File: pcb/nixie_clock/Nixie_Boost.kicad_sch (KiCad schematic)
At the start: 0 parts

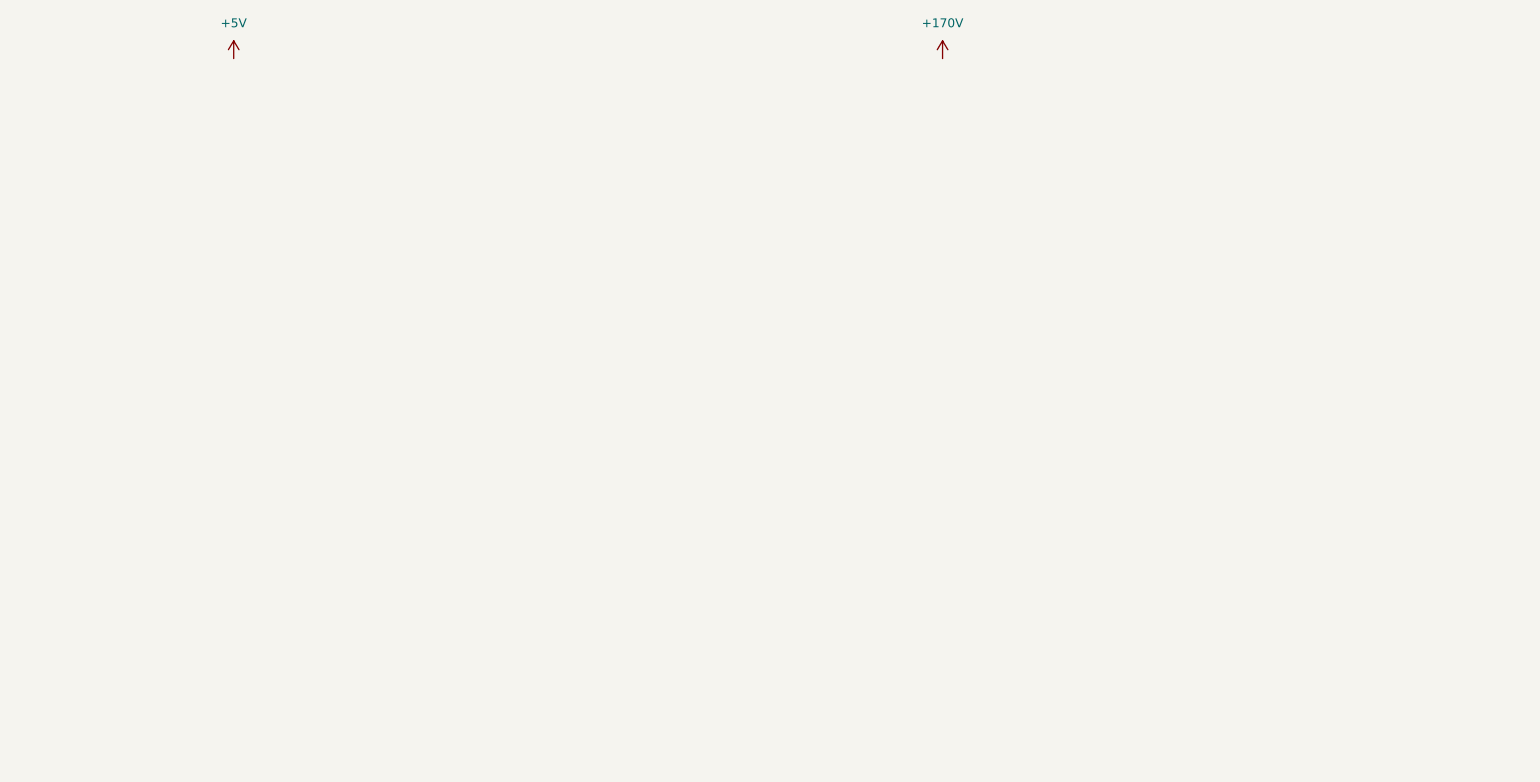
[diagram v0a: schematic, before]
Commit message: schematic finalisation, footprint assignment and start on placeing components in layout.
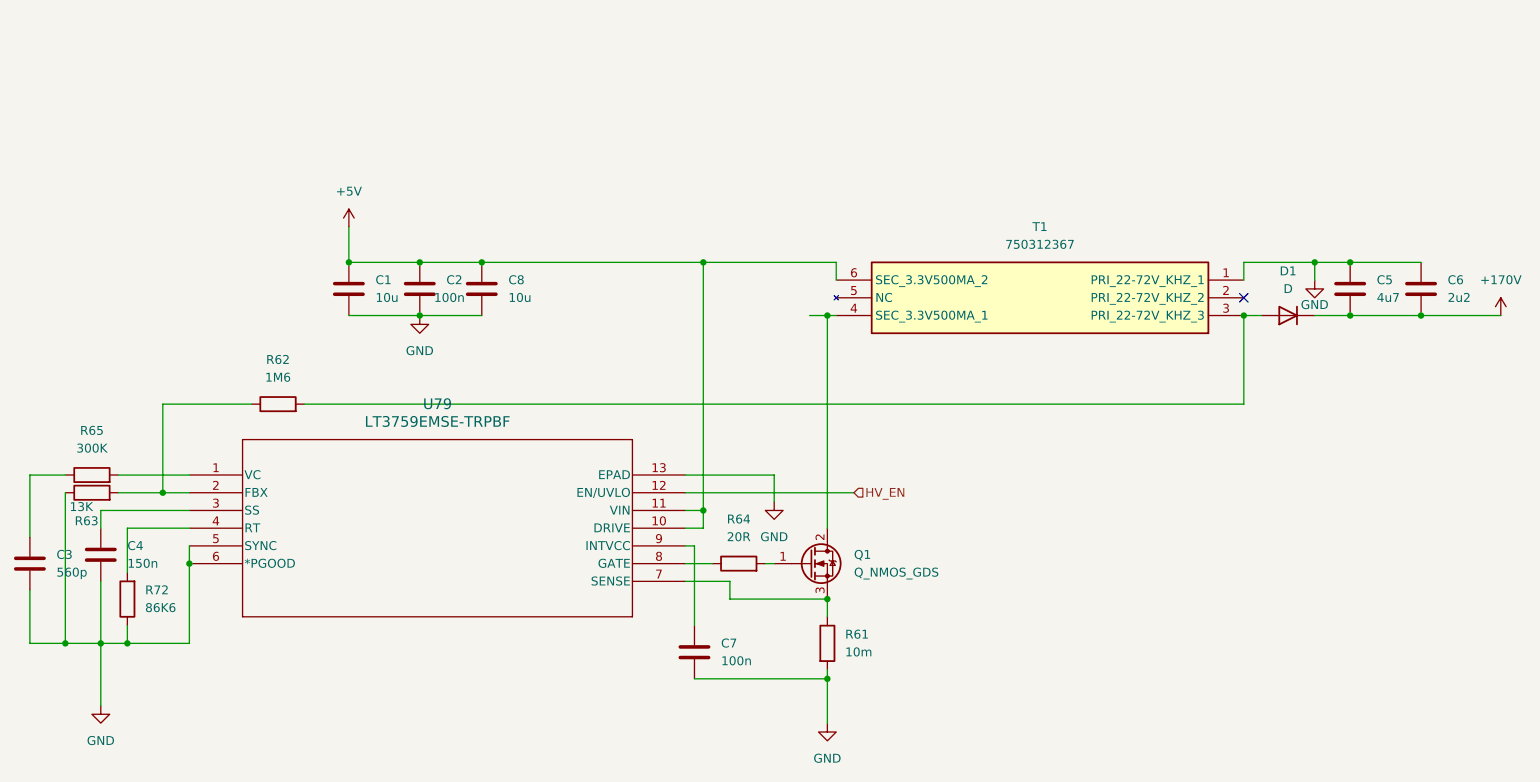
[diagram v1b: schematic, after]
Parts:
- added C1, C8: 10u, Capacitor_SMD:C_1210_3225Metric, symbol Device:C
- added C2: 100n, Capacitor_SMD:C_0805_2012Metric, symbol Device:C
- added C3: 560p, Capacitor_SMD:C_0603_1608Metric, symbol Device:C
- added C4: 150n, Capacitor_SMD:C_0603_1608Metric, symbol Device:C
- added C5: 4u7, Capacitor_SMD:C_0603_1608Metric, symbol Device:C
- added C6: 2u2, Capacitor_SMD:C_2220_5750Metric, symbol Device:C
- added C7: 100n, Capacitor_SMD:C_1812_4532Metric, symbol Device:C
- added D1: D, Capacitor_SMD:C_1812_4532Metric, symbol Device:D
- added Q1: Q_NMOS_GDS, Package_TO_SOT_SMD:LFPAK56, symbol Device:Q_NMOS_GDS
- added R61: 10m, Resistor_SMD:R_0805_2012Metric, symbol Device:R
- added R62: 1M6, Resistor_SMD:R_0603_1608Metric, symbol Device:R
- added R63: 13K, Resistor_SMD:R_0603_1608Metric, symbol Device:R
- added R64: 20R, Resistor_SMD:R_0603_1608Metric, symbol Device:R
- added R65: 300K, Resistor_SMD:R_0603_1608Metric, symbol Device:R
- added R72: 86K6, Resistor_SMD:R_0603_1608Metric, symbol Device:R
- added T1: 750312367, 750312367, symbol 750312367:750312367
- added U79: LT3759EMSE-TRPBF, MSOP-12_MSE_LIT, symbol 2024-10-24_20-25-09:LT3759EMSE-TRPBF
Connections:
- net +170V: now also C5.2, C6.2, D1.1 (K)
- net +5V: now also C1.1, C2.1, C8.1, T1.6 (SEC_3.3V500MA_2), U79.10 (DRIVE), U79.11 (VIN)
- new net: R62.1, R63.2, U79.2 (FBX)
- new net: Q1.1 (G), R64.2
- new net: Q1.2 (D), T1.4 (SEC_3.3V500MA_1)
- new net: Q1.3 (S), R61.1, U79.7 (SENSE)
- new net: D1.2 (A), R62.2, T1.3 (PRI_22-72V_KHZ_3)
- new net: C3.1, R65.1
- new net: R65.2, U79.1 (VC)
- new net: R72.2, U79.4 (RT)
- new net: R64.1, U79.8 (GATE)
- new net: C4.2, U79.3 (SS)
- new net: C7.1, U79.9 (INTVCC)
- new net GND: C1.2, C2.2, C3.2, C4.1, C5.1, C6.1, C7.2, C8.2, R61.2, R63.1, R72.1, T1.1 (PRI_22-72V_KHZ_1), U79.13 (EPAD), U79.5 (SYNC), U79.6 (*PGOOD)
- new net HV_EN: U79.12 (EN/UVLO)
- no-connect marks 0 -> 1

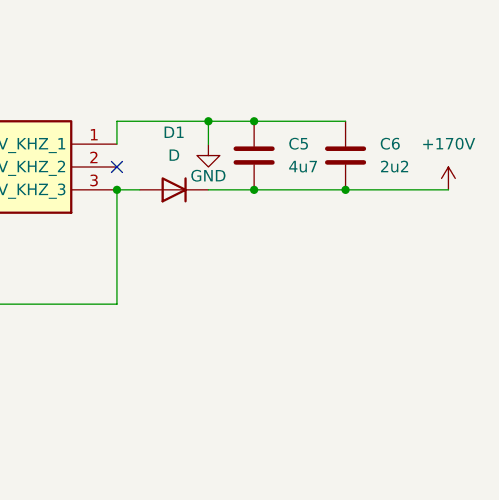
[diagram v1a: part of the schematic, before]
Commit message: finalization of schematic (might add fuze on 170v supply) looking at pcb routing now. Decided on 6 layers.
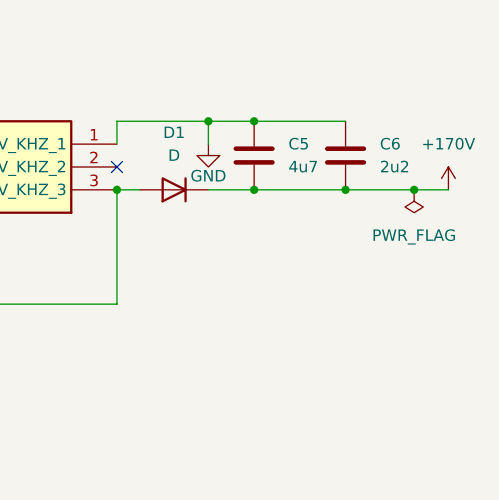
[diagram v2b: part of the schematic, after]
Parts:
- T1: footprint 750312367 -> 750312367:750312367
- U79: footprint MSOP-12_MSE_LIT -> LT3759EMSE:MSOP-12_MSE_LIT
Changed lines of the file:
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@@
+	)
+	(junction
+		(at 254 100.33)
+		(diameter 0)
+		(color 0 0 0 0)
 	)
 	(junction
@@
 	(wire
 		(pts
+			(xy 254 100.33) (xy 257.81 100.33)
+		)
+		(stroke
+			(width 0)
+			(type default)
+		)
+	)
+	(wire
+		(pts
 			(xy 140.97 135.89) (xy 144.78 135.89)
 		)
@@
 	(wire
 		(pts
-			(xy 246.38 100.33) (xy 257.81 100.33)
+			(xy 246.38 100.33) (xy 254 100.33)
 		)
 		(stroke
@@
 			)
 		)
-		(property "Footprint" "750312367"
+		(property "Footprint" "750312367:750312367"
 			(at 166.37 5.41 0)
 			(effects
@@
 	)
 	(symbol
+		(lib_id "power:PWR_FLAG")
+		(at 254 100.33 180)
+		(unit 1)
+		(exclude_from_sim no)
+		(in_bom yes)
+		(on_board yes)
+		(dnp no)
+		(fields_autoplaced yes)
+		(property "Reference" "#FLG01"
+			(at 254 102.235 0)
+			(effects
+				(font
+					(size 1.27 1.27)
+				)
+				(hide yes)
+			)
+		)
+		(property "Value" "PWR_FLAG"
+			(at 254 105.41 0)
+			(effects
+				(font
+					(size 1.27 1.27)
+				)
+			)
+		)
+		(property "Footprint" ""
+			(at 254 100.33 0)
+			(effects
+				(font
+					(size 1.27 1.27)
+				)
+				(hide yes)
+			)
+		)
+		(property "Datasheet" "~"
+			(at 254 100.33 0)
+			(effects
+				(font
+					(size 1.27 1.27)
+				)
+				(hide yes)
+			)
+		)
+		(property "Description" "Special symbol for telling ERC where power comes from"
+			(at 254 100.33 0)
+			(effects
+				(font
+					(size 1.27 1.27)
+				)
+				(hide yes)
+			)
+		)
+		(pin "1"
+		)
+		(instances
+			(project ""
+				(path "/87768a79-2a56-4b5f-a764-e1a4021de947/c1bb63d0-0983-4b38-93d5-e35be1909e08"
+					(reference "#FLG01")
+					(unit 1)
+				)
+			)
+		)
+	)
+	(symbol
 		(lib_id "Device:C")
 		(at 111.76 96.52 0)
@@
 			)
 		)
-		(property "Footprint" "MSOP-12_MSE_LIT"
+		(property "Footprint" "LT3759EMSE:MSOP-12_MSE_LIT"
 			(at 69.85 123.19 0)
 			(effects

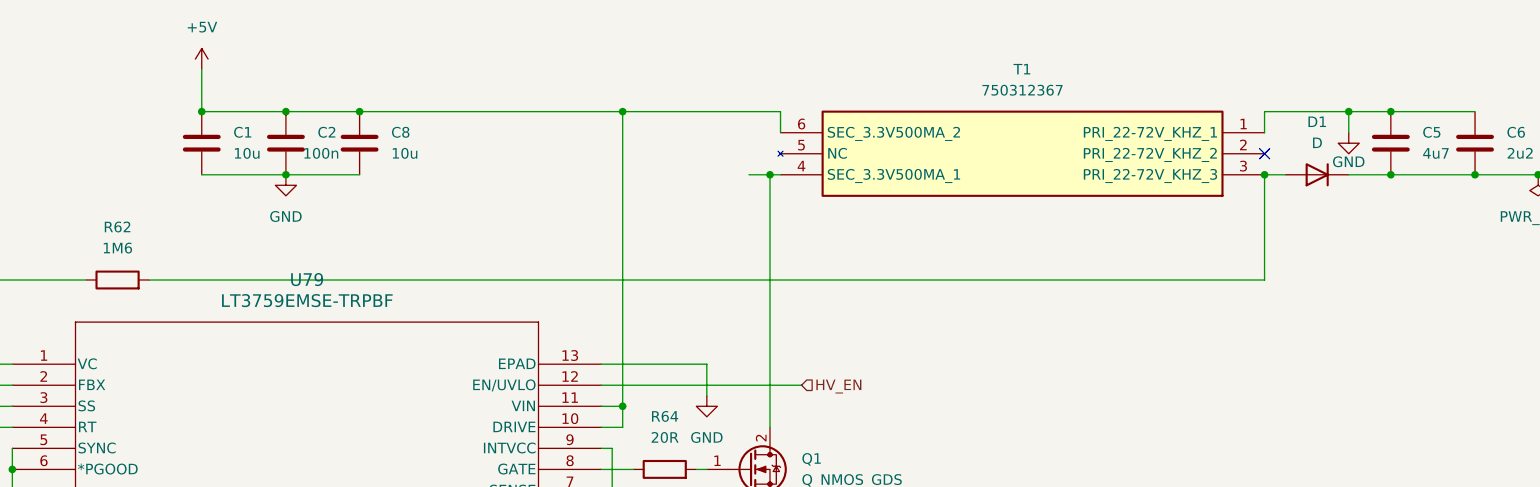
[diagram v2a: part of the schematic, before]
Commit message: hierarkical pcb switch and finishing of layout time for final checks need to redo nixie tube layout
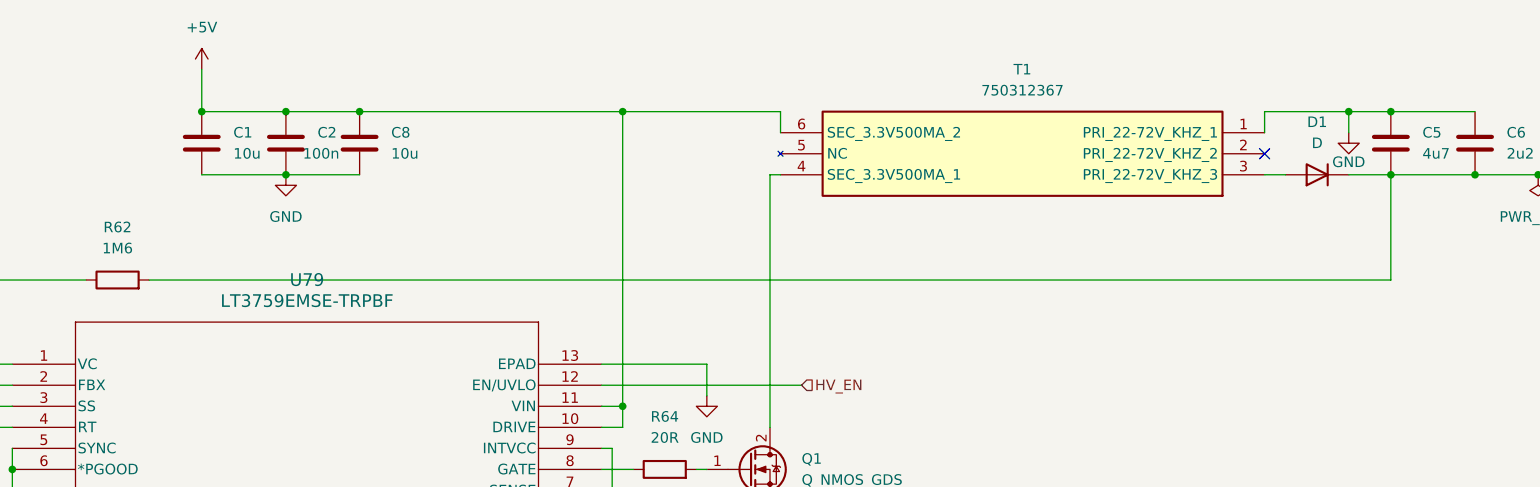
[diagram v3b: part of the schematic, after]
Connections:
- net +170V: now also R62.2
- net at D1.2 (A), T1.3 (PRI_22-72V_KHZ_3): no longer R62.2
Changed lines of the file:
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@@
-	)
-	(junction
-		(at 161.29 100.33)
-		(diameter 0)
-		(color 0 0 0 0)
 	)
 	(junction
@@
 	(junction
 		(at 60.96 147.32)
-		(diameter 0)
-		(color 0 0 0 0)
-	)
-	(junction
-		(at 220.98 100.33)
 		(diameter 0)
 		(color 0 0 0 0)
@@
 	(wire
 		(pts
+			(xy 236.22 113.03) (xy 236.22 100.33)
+		)
+		(stroke
+			(width 0)
+			(type default)
+		)
+	)
+	(wire
+		(pts
 			(xy 60.96 130.81) (xy 60.96 137.16)
 		)
@@
 	(wire
 		(pts
-			(xy 220.98 113.03) (xy 86.36 113.03)
+			(xy 86.36 113.03) (xy 236.22 113.03)
 		)
 		(stroke
@@
 	(wire
 		(pts
-			(xy 220.98 100.33) (xy 220.98 113.03)
-		)
-		(stroke
-			(width 0)
-			(type default)
-		)
-	)
-	(wire
-		(pts
 			(xy 111.76 92.71) (xy 143.51 92.71)
-		)
-		(stroke
-			(width 0)
-			(type default)
-		)
-	)
-	(wire
-		(pts
-			(xy 158.75 100.33) (xy 161.29 100.33)
 		)
 		(stroke
@@
 			)
 			(justify left)
+		)
+	)
+	(netclass_flag ""
+		(length 2.54)
+		(shape round)
+		(at 223.52 100.33 180)
+		(fields_autoplaced yes)
+		(effects
+			(font
+				(size 1.27 1.27)
+			)
+			(justify right bottom)
+		)
+		(property "Netclass" "power"
+			(at 224.2185 102.87 0)
+			(effects
+				(font
+					(size 1.27 1.27)
+					(italic yes)
+				)
+				(justify left)
+			)
+		)
+	)
+	(netclass_flag ""
+		(length 2.54)
+		(shape round)
+		(at 161.29 109.22 90)
+		(fields_autoplaced yes)
+		(effects
+			(font
+				(size 1.27 1.27)
+			)
+			(justify left bottom)
+		)
+		(property "Netclass" "power"
+			(at 158.75 108.5215 90)
+			(effects
+				(font
+					(size 1.27 1.27)
+					(italic yes)
+				)
+				(justify left)
+			)
+		)
+	)
+	(netclass_flag ""
+		(length 2.54)
+		(shape round)
+		(at 154.94 140.97 180)
+		(fields_autoplaced yes)
+		(effects
+			(font
+				(size 1.27 1.27)
+			)
+			(justify right bottom)
+		)
+		(property "Netclass" "power"
+			(at 155.6385 143.51 0)
+			(effects
+				(font
+					(size 1.27 1.27)
+					(italic yes)
+				)
+				(justify left)
+			)
 		)
 	)
@@
 			)
 		)
-		(property "Datasheet" "~"
+		(property "Datasheet" "https://assets.nexperia.com/documents/data-sheet/PSMN014-80YL.pdf"
 			(at 158.75 135.89 0)
 			(effects

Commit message: 3d models done
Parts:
- T1: LCSC Part # (none) -> C17357180
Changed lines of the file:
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@@
+			)
+		)
+		(property "LCSC Part #" "C17357180"
+			(at 220.98 100.33 0)
+			(effects
+				(font
+					(size 1.27 1.27)
+				)
+				(hide yes)
 			)
 		)

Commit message: fixing some issues.
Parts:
- C1, C8: LCSC Part # (none) -> C6477141
- C2: LCSC Part # (none) -> C2170365
- C3: LCSC Part # (none) -> C2171678
- C4: LCSC Part # (none) -> C3844381
- C5: LCSC Part # (none) -> C3842329
- C6: LCSC Part # (none) -> C2168251
- C7: LCSC Part # (none) -> C2179130
- D1: footprint Capacitor_SMD:C_1812_4532Metric -> Diode_SMD:D_SOD-123; LCSC Part # (none) -> C17550678
- Q1: LCSC Part # (none) -> C3282674
- R61: LCSC Part # (none) -> C2977779
- R62: LCSC Part # (none) -> C2091296
- R63: LCSC Part # (none) -> C402966
- R64: LCSC Part # (none) -> C400657
- R65: LCSC Part # (none) -> C278615
- R72: LCSC Part # (none) -> C2094634
- U79: value LT3759EMSE-TRPBF -> LT3759EMSE#TRPBF; LCSC Part # (none) -> C580139
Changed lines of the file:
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@@
+			)
+		)
+		(property "LCSC Part #" "C402966"
+			(at 55.88 125.73 0)
+			(effects
+				(font
+					(size 1.27 1.27)
+				)
+				(hide yes)
 			)
 		)
@@
 			)
 		)
+		(property "LCSC Part #" "C3282674"
+			(at 158.75 135.89 0)
+			(effects
+				(font
+					(size 1.27 1.27)
+				)
+				(hide yes)
+			)
+		)
 		(pin "3"
 		)
@@
 			)
 		)
+		(property "LCSC Part #" "C278615"
+			(at 55.88 123.19 0)
+			(effects
+				(font
+					(size 1.27 1.27)
+				)
+				(hide yes)
+			)
+		)
 		(pin "1"
 		)
@@
 			)
 		)
+		(property "LCSC Part #" "C2094634"
+			(at 60.96 140.97 0)
+			(effects
+				(font
+					(size 1.27 1.27)
+				)
+				(hide yes)
+			)
+		)
 		(pin "1"
 		)
@@
 			)
 		)
+		(property "LCSC Part #" "C400657"
+			(at 148.59 135.89 0)
+			(effects
+				(font
+					(size 1.27 1.27)
+				)
+				(hide yes)
+			)
+		)
 		(pin "1"
 		)
@@
 			)
 		)
+		(property "LCSC Part #" "C2168251"
+			(at 246.38 96.52 0)
+			(effects
+				(font
+					(size 1.27 1.27)
+				)
+				(hide yes)
+			)
+		)
 		(pin "2"
 		)
@@
 			)
 		)
-		(property "Footprint" "Capacitor_SMD:C_1812_4532Metric"
+		(property "Footprint" "Diode_SMD:D_SOD-123"
 			(at 227.33 100.33 0)
 			(effects
@@
 			)
 		)
+		(property "LCSC Part #" "C17550678"
+			(at 227.33 100.33 0)
+			(effects
+				(font
+					(size 1.27 1.27)
+				)
+				(hide yes)
+			)
+		)
 		(pin "1"
 		)
@@
 			)
 		)
+		(property "LCSC Part #" "C2171678"
+			(at 46.99 135.89 0)
+			(effects
+				(font
+					(size 1.27 1.27)
+				)
+				(hide yes)
+			)
+		)
 		(pin "2"
 		)
@@
 			)
 		)
+		(property "LCSC Part #" "C6477141"
+			(at 92.71 96.52 0)
+			(effects
+				(font
+					(size 1.27 1.27)
+				)
+				(hide yes)
+			)
+		)
 		(pin "1"
 		)
@@
 			)
 		)
+		(property "LCSC Part #" "C3844381"
+			(at 57.15 134.62 0)
+			(effects
+				(font
+					(size 1.27 1.27)
+				)
+				(hide yes)
+			)
+		)
 		(pin "2"
 		)
@@
 			)
 		)
+		(property "LCSC Part #" "C3842329"
+			(at 236.22 96.52 0)
+			(effects
+				(font
+					(size 1.27 1.27)
+				)
+				(hide yes)
+			)
+		)
 		(pin "2"
 		)
@@
 			)
 		)
+		(property "LCSC Part #" "C2091296"
+			(at 82.55 113.03 0)
+			(effects
+				(font
+					(size 1.27 1.27)
+				)
+				(hide yes)
+			)
+		)
 		(pin "1"
 		)
@@
 			)
 		)
+		(property "LCSC Part #" "C2170365"
+			(at 102.87 96.52 0)
+			(effects
+				(font
+					(size 1.27 1.27)
+				)
+				(hide yes)
+			)
+		)
 		(pin "1"
 		)
@@
 			)
 		)
+		(property "LCSC Part #" "C2977779"
+			(at 161.29 147.32 0)
+			(effects
+				(font
+					(size 1.27 1.27)
+				)
+				(hide yes)
+			)
+		)
 		(pin "1"
 		)
@@
 			)
 		)
+		(property "LCSC Part #" "C6477141"
+			(at 111.76 96.52 0)
+			(effects
+				(font
+					(size 1.27 1.27)
+				)
+				(hide yes)
+			)
+		)
 		(pin "2"
 		)
@@
 			)
 		)
-		(property "Value" "LT3759EMSE-TRPBF"
+		(property "Value" "LT3759EMSE#TRPBF"
 			(at 105.41 115.57 0)
 			(effects
@@
 			)
 		)
-		(property "Datasheet" "LT3759EMSE-TRPBF"
+		(property "Datasheet" "LT3759EMSE#TRPBF"
 			(at 69.85 123.19 0)
 			(effects
@@
 			)
 		)
+		(property "LCSC Part #" "C580139"
+			(at 69.85 123.19 0)
+			(effects
+				(font
+					(size 1.27 1.27)
+				)
+				(hide yes)
+			)
+		)
 		(pin "1"
 		)
@@
 			(at 142.24 148.59 0)
 			(effects
+				(font
+					(size 1.27 1.27)
+				)
+				(hide yes)
+			)
+		)
+		(property "LCSC Part #" "C2179130"
+			(at 142.24 148.59 0)
+			(effects
